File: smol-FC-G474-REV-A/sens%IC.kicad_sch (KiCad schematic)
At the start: 0 parts

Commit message: Added whole new schematic (sensors, OSD, Blackbox), changed text in cubemx
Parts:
- added C15, C16, C17, C18, C24, C26, C27, C28: 100n, symbol Device:C_Small
- added C19, C20: 10p, symbol Device:C_Small
- added C21, C22: 47u, symbol Device:C_Polarized_Small
- added C23: 2u2, symbol Device:C_Small
- added C25: 10n, symbol Device:C_Small
- added R13, R14: 75, symbol Device:R_Small
- added R15, R16, R17: 10K, symbol Device:R_Small
- added U3: AT7456E, MAX7456EUI_:SOP65P637X110-28N, symbol MAX7456EUI_:MAX7456EUI_
- added U4: ICM-42688-P, ICM-42688-P:PQFN50P300X250X97-14N, symbol ICM-42688-P:ICM-42688-P
- added U5: DPS368XTSA1, DPS368XTSA1:XDCR_DPS368XTSA1, symbol DPS368XTSA1:DPS368XTSA1
- added U6: W25Q128JVSIQ, W25Q128JVSIQ:SOIC127P790X216-8N, symbol W25Q128JVSIQ:W25Q128JVSIQ
- added Y2: 27MHz, symbol Device:Crystal_GND24
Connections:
- new net: C22.1, U3.25 (SAG)
- new net: C21.1, U3.26 (VOUT)
- new net: C21.2, C22.2, R14.1
- new net +3V3_CORE: C28.1, R17.1, U6.3 (/WP(IO2)), U6.7 (/HOLD/RESET(IO3)), U6.8 (VCC)
- new net +3V3_SENS: C23.1, C24.1, C25.1, C26.1, C27.1, R15.1, R16.1, U4.5 (VDDIO), U4.8 (VDD), U5.6 (VDDIO), U5.8 (VDD)
- new net +5V: C15.1, C16.1, C17.1, U3.21 (AVDD), U3.24 (PVDD), U3.3 (DVDD)
- new net GND: C15.2, C16.2, C17.2, C19.2, C20.2, C23.2, C24.2, C25.2, C26.2, C27.2, C28.2, R13.2, U3.20 (AGND), U3.23 (PGND), U3.29 (EP), U3.4 (DGND), U4.11 (RESV_11), U4.6 (GND), U4.7 (RESV_7), U5.1 (GND), U5.7 (GND), U6.4 (GND), Y2.2 (G), Y2.4 (G)
- new net I2C4_SCL: R16.2, U5.4 (SCK)
- new net I2C4_SDA: R15.2, U5.3 (SDI)
- new net IMU_IRQ: U4.4 (INT1/INT)
- new net OSD_CLKIN: C19.1, U3.5 (CLKIN), Y2.1
- new net OSD_VIN: C18.2, U3.22 (VIN)
- new net OSD_XFB: C20.1, U3.6 (XFB), Y2.3
- new net SPI1_CS: U3.8 (~{CS})
- new net SPI1_MISO: U3.11 (SDOUT)
- new net SPI1_MOSI: U3.9 (SDIN)
- new net SPI1_SCK: U3.10 (SCLK)
- new net SPI2_CS: U4.12 (AP_CS)
- new net SPI2_MISO: U4.1 (AP_SDO/AP_AD0)
- new net SPI2_MOSI: U4.14 (AP_SDA/AP_SDIO/AP_SDI)
- new net SPI2_SCK: U4.13 (AP_SCL/AP_SCLK)
- new net SPI3_CS: R17.2, U6.1 (/CS)
- new net SPI3_MISO: U6.2 (DO(IO1))
- new net SPI3_MOSI: U6.5 (DI(IO0))
- new net SPI3_SCK: U6.6 (CLK)
- new net VIDEO_IN: C18.1, R13.1
- new net VIDEO_OUT: R14.2
- no-connect marks 0 -> 7
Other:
- note added: "BARO"
- note added: "Blackbox"
- note added: "IMU"
- note added: "OSD"

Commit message: complete connectors layout and initialize buck converter section. Added buck docs in /docs.
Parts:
- R15, R16: value 10K -> 4.7K
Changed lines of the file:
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@@
 	(title_block
 		(title "smol-FC-G474")
-		(date "2026-05-24")
-		(rev "0.0.1")
+		(date "2026-05-31")
+		(rev "0.7.0")
 		(company "Daniel Plewa")
 		(comment 1 "License: CERN-OHL-W v2")
@@
 			)
 		)
-		(property "Value" "10K"
+		(property "Value" "4.7K"
 			(at 92.456 145.542 0)
 			(show_name no)
@@
 			)
 		)
-		(property "Value" "10K"
+		(property "Value" "4.7K"
 			(at 100.076 145.542 0)
 			(show_name no)

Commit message: Updated Buck-5V doc, added Buck 5V/10V and LDO for 3v3 on schematic
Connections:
- net +5V is gone; now on net +5V_SYS: C15.1, C16.1, C17.1, U3.21 (AVDD), U3.24 (PVDD), U3.3 (DVDD)
- net GND: now also U4.9 (INT2/FSYNC/CLKIN)
- net +5V_SYS: now reaches U3.19 (~{RESET})
- net OSD_SAG: now reaches C22.1, U3.25 (SAG)
- net OSD_VOUT: now reaches C21.1, U3.26 (VOUT)
- no-connect marks 7 -> 6
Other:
- moved on the sheet: C21, C22, C23, C24, C25, R14

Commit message: Changed 10V buck to 9V buck
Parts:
- U3: footprint MAX7456EUI_:SOP65P637X110-28N -> (none)
- U4: footprint ICM-42688-P:PQFN50P300X250X97-14N -> (none)
- U5: footprint DPS368XTSA1:XDCR_DPS368XTSA1 -> (none)
- U6: footprint W25Q128JVSIQ:SOIC127P790X216-8N -> (none)
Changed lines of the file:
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@@
 			)
 		)
-		(property "Footprint" "DPS368XTSA1:XDCR_DPS368XTSA1"
+		(property "Footprint" ""
 			(at 69.088 133.35 0)
 			(hide yes)
@@
 			)
 		)
-		(property "Footprint" "W25Q128JVSIQ:SOIC127P790X216-8N"
+		(property "Footprint" ""
 			(at 241.046 78.232 0)
 			(hide yes)
@@
 			)
 		)
-		(property "Footprint" "ICM-42688-P:PQFN50P300X250X97-14N"
+		(property "Footprint" ""
 			(at 228.092 12.954 0)
 			(hide yes)
@@
 			)
 		)
-		(property "Footprint" "MAX7456EUI_:SOP65P637X110-28N"
+		(property "Footprint" ""
 			(at 80.772 40.132 0)
 			(hide yes)

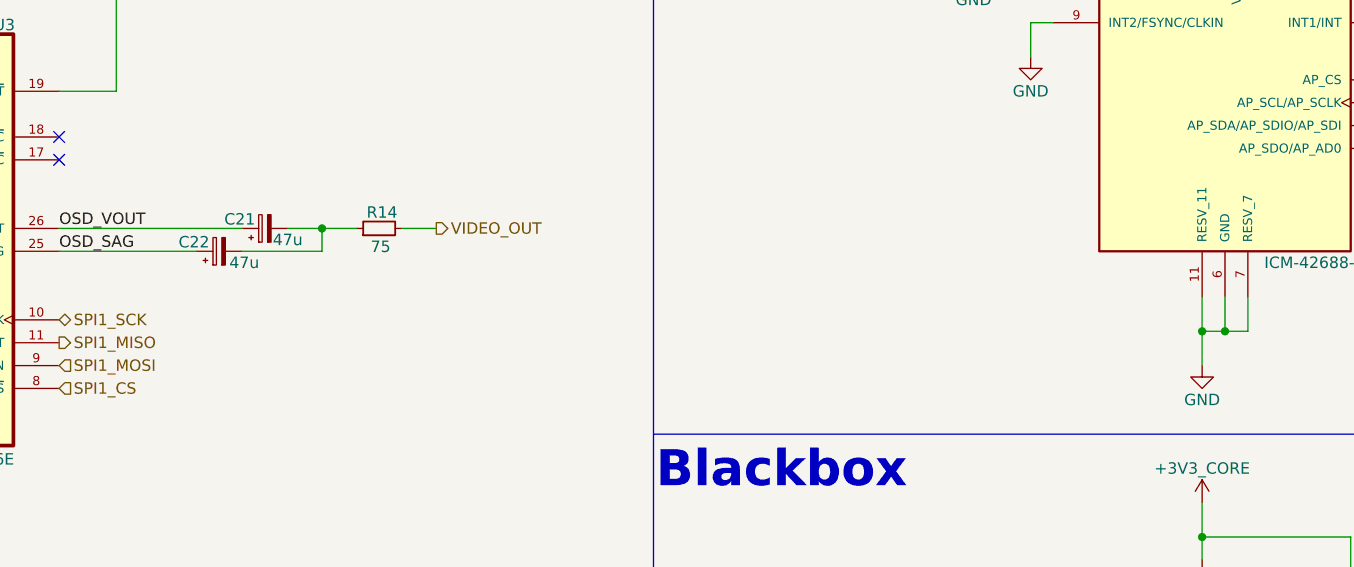
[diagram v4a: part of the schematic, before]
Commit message: Attached footprints and finalized schematic.
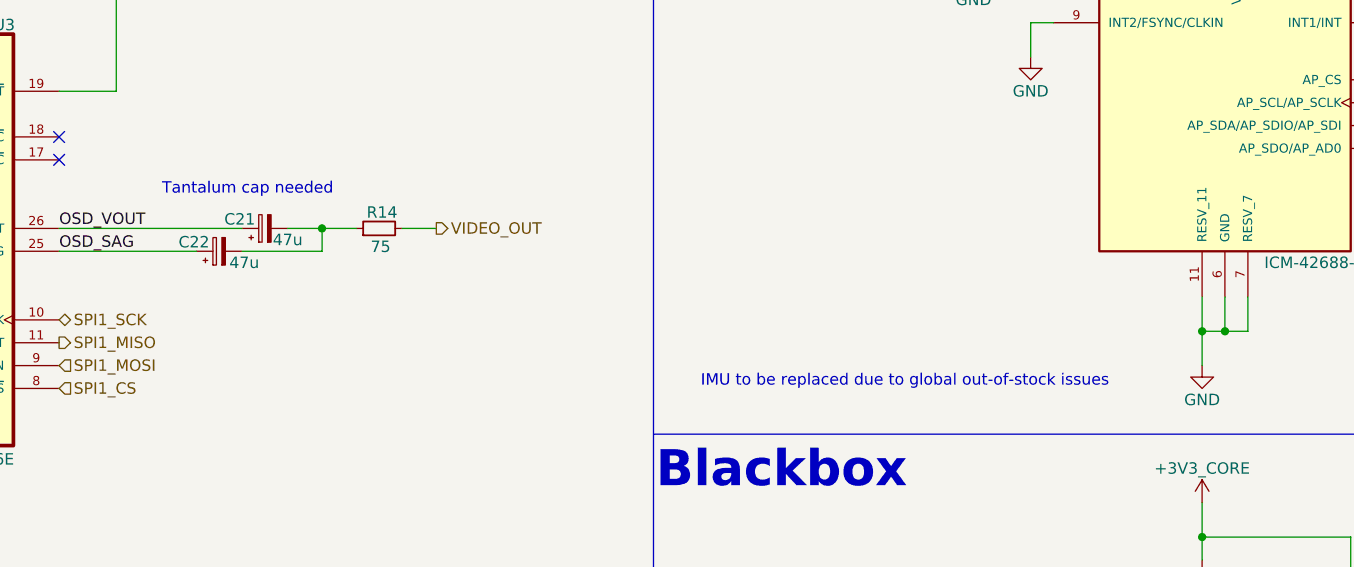
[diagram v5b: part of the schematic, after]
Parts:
- C15, C16, C17, C18, C19, C20, C23, C24, C25, C26, C27, C28: footprint (none) -> Capacitor_SMD:C_0402_1005Metric
- C21, C22: footprint (none) -> Capacitor_SMD:C_1206_3216Metric
- R13, R14, R15, R16, R17: footprint (none) -> Resistor_SMD:R_0402_1005Metric
- U3: footprint (none) -> AT7456E:SOP65P637X110-28N
- U4: footprint (none) -> ICM-42688-P:PQFN50P300X250X97-14N
- U5: footprint (none) -> DPS368XTSA1:XDCR_DPS368XTSA1
- U6: footprint (none) -> W25Q128JVSIQ:SOIC127P790X216-8N
- Y2: footprint (none) -> SX1B27.000F0810F30:XTAL_TSX-3225_16.0000MF18X-AC3
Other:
- note added: "IMU to be replaced due to global out-of-stock issues"
- note added: "Tantalum cap needed"
- title: smol-FC-G474 -> smol-FC-G474-REV-A
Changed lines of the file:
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@@
 	(paper "A4")
 	(title_block
-		(title "smol-FC-G474")
-		(date "2026-05-31")
-		(rev "0.7.0")
+		(title "smol-FC-G474-REV-A")
+		(date "2026-06-05")
+		(rev "0.9.3")
 		(company "Daniel Plewa")
 		(comment 1 "License: CERN-OHL-W v2")
 		(comment 2 "GitHub: https://github.com/Def12345678/smol-FC-G474-REV-A")
-		(comment 3 "BEC 5A/2A, 10V/2A | Baro, OSD Chip and 16MB blackbox")
+		(comment 3 "BEC 5A/3A, 10V/3A | Baro, OSD Chip and 16MB blackbox")
 		(comment 4 "Open source flight controller on STM32G4, 20x20 3.5mm hole")
 	)
@@
 		)
 	)
+	(text "Tantalum cap needed"
+		(exclude_from_sim no)
+		(at 110.49 64.262 0)
+		(effects
+			(font
+				(size 1.27 1.27)
+			)
+			(justify left)
+		)
+	)
 	(text "IMU"
 		(exclude_from_sim no)
@@
 		)
 	)
+	(text "IMU to be replaced due to global out-of-stock issues"
+		(exclude_from_sim no)
+		(at 193.04 85.598 0)
+		(effects
+			(font
+				(size 1.27 1.27)
+			)
+		)
+	)
 	(text "OSD"
 		(exclude_from_sim no)
@@
 			)
 		)
-		(property "Footprint" ""
+		(property "Footprint" "Capacitor_SMD:C_0402_1005Metric"
 			(at 57.15 29.21 0)
 			(hide yes)
@@
 			)
 		)
-		(property "Footprint" ""
+		(property "Footprint" "Capacitor_SMD:C_0402_1005Metric"
 			(at 41.91 140.97 0)
 			(hide yes)
@@
 			)
 		)
-		(property "Footprint" ""
+		(property "Footprint" "Capacitor_SMD:C_0402_1005Metric"
 			(at 250.19 29.21 0)
 			(hide yes)
@@
 			)
 		)
-		(property "Footprint" ""
+		(property "Footprint" "DPS368XTSA1:XDCR_DPS368XTSA1"
 			(at 69.088 133.35 0)
 			(hide yes)
@@
 			)
 		)
-		(property "Footprint" ""
+		(property "Footprint" "Capacitor_SMD:C_0402_1005Metric"
 			(at 46.99 29.21 0)
 			(hide yes)
@@
 			)
 		)
-		(property "Footprint" ""
+		(property "Footprint" "W25Q128JVSIQ:SOIC127P790X216-8N"
 			(at 241.046 78.232 0)
 			(hide yes)
@@
 			)
 		)
-		(property "Footprint" ""
+		(property "Footprint" "ICM-42688-P:PQFN50P300X250X97-14N"
 			(at 228.092 12.954 0)
 			(hide yes)
@@
 			)
 		)
-		(property "Footprint" ""
+		(property "Footprint" "Capacitor_SMD:C_0402_1005Metric"
 			(at 67.31 29.21 0)
 			(hide yes)
@@
 			)
 		)
-		(property "Footprint" ""
+		(property "Footprint" "Capacitor_SMD:C_0402_1005Metric"
 			(at 52.07 97.79 0)
 			(hide yes)
@@
 			)
 		)
-		(property "Footprint" ""
+		(property "Footprint" "Capacitor_SMD:C_0402_1005Metric"
 			(at 35.56 53.34 0)
 			(hide yes)
@@
 			)
 		)
-		(property "Footprint" ""
+		(property "Footprint" "Capacitor_SMD:C_0402_1005Metric"
 			(at 200.66 29.21 0)
 			(hide yes)
@@
 			)
 		)
-		(property "Footprint" ""
+		(property "Footprint" "AT7456E:SOP65P637X110-28N"
 			(at 80.772 40.132 0)
 			(hide yes)
@@
 			)
 		)
-		(property "Footprint" ""
+		(property "Footprint" "Resistor_SMD:R_0402_1005Metric"
 			(at 91.44 144.78 0)
 			(hide yes)
@@
 			)
 		)
-		(property "Footprint" ""
+		(property "Footprint" "Capacitor_SMD:C_0402_1005Metric"
 			(at 52.07 140.97 0)
 			(hide yes)
@@
 			)
 		)
-		(property "Footprint" ""
+		(property "Footprint" "Capacitor_SMD:C_1206_3216Metric"
 			(at 121.92 68.58 0)
 			(hide yes)
@@
 			)
 		)
-		(property "Footprint" ""
+		(property "Footprint" "Capacitor_SMD:C_0402_1005Metric"
 			(at 34.29 97.79 0)
 			(hide yes)
@@
 			)
 		)
-		(property "Footprint" ""
+		(property "Footprint" "SX1B27.000F0810F30:XTAL_TSX-3225_16.0000MF18X-AC3"
 			(at 43.18 90.17 0)
 			(hide yes)
@@
 			)
 		)
-		(property "Footprint" ""
+		(property "Footprint" "Resistor_SMD:R_0402_1005Metric"
 			(at 99.06 144.78 0)
 			(hide yes)
@@
 			)
 		)
-		(property "Footprint" ""
+		(property "Footprint" "Resistor_SMD:R_0402_1005Metric"
 			(at 265.43 116.84 0)
 			(hide yes)
@@
 			)
 		)
-		(property "Footprint" ""
+		(property "Footprint" "Capacitor_SMD:C_0402_1005Metric"
 			(at 210.82 29.21 0)
 			(hide yes)
@@
 			)
 		)
-		(property "Footprint" ""
+		(property "Footprint" "Capacitor_SMD:C_0402_1005Metric"
 			(at 226.06 107.95 0)
 			(hide yes)
@@
 			)
 		)
-		(property "Footprint" ""
+		(property "Footprint" "Resistor_SMD:R_0402_1005Metric"
 			(at 134.62 68.58 0)
 			(hide yes)
@@
 			)
 		)
-		(property "Footprint" ""
+		(property "Footprint" "Capacitor_SMD:C_1206_3216Metric"
 			(at 116.84 71.12 0)
 			(hide yes)
@@
 			)
 		)
-		(property "Footprint" ""
+		(property "Footprint" "Resistor_SMD:R_0402_1005Metric"
 			(at 29.21 59.69 0)
 			(hide yes)
